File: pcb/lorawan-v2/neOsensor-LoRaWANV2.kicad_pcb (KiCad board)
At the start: 2 copper layers, 49.5 x 49.5 mm, 35 parts, among them J1 Conn_01x05, J2 Conn_01x02, J3 Conn_01x05, J4 Conn_01x04, J5 Conn_01x05, J6 Conn_01x05, J7 Conn_01x05, SW1 G71Y, U1 OLED1.3_I2C, U2 ATECC508A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

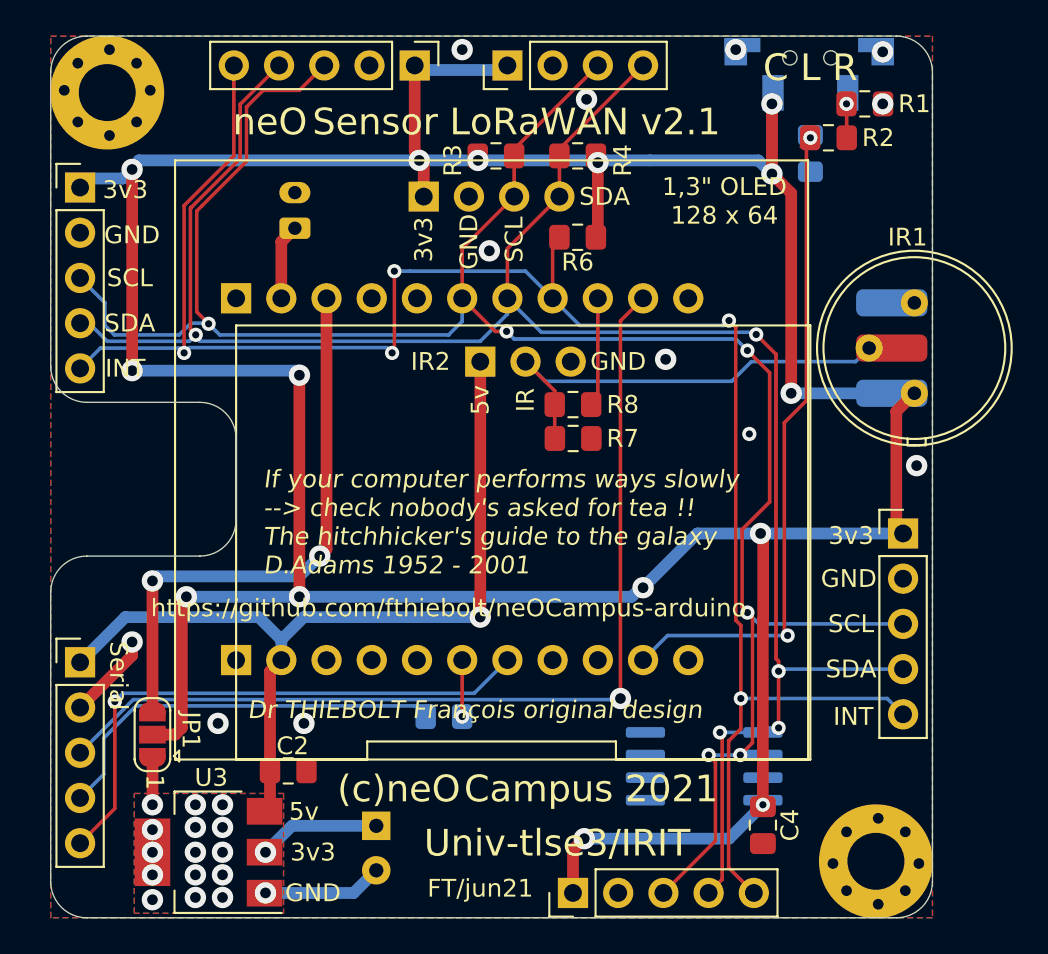
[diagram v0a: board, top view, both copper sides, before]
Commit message: new LoRaWAN V2.1 sent to manufacturing
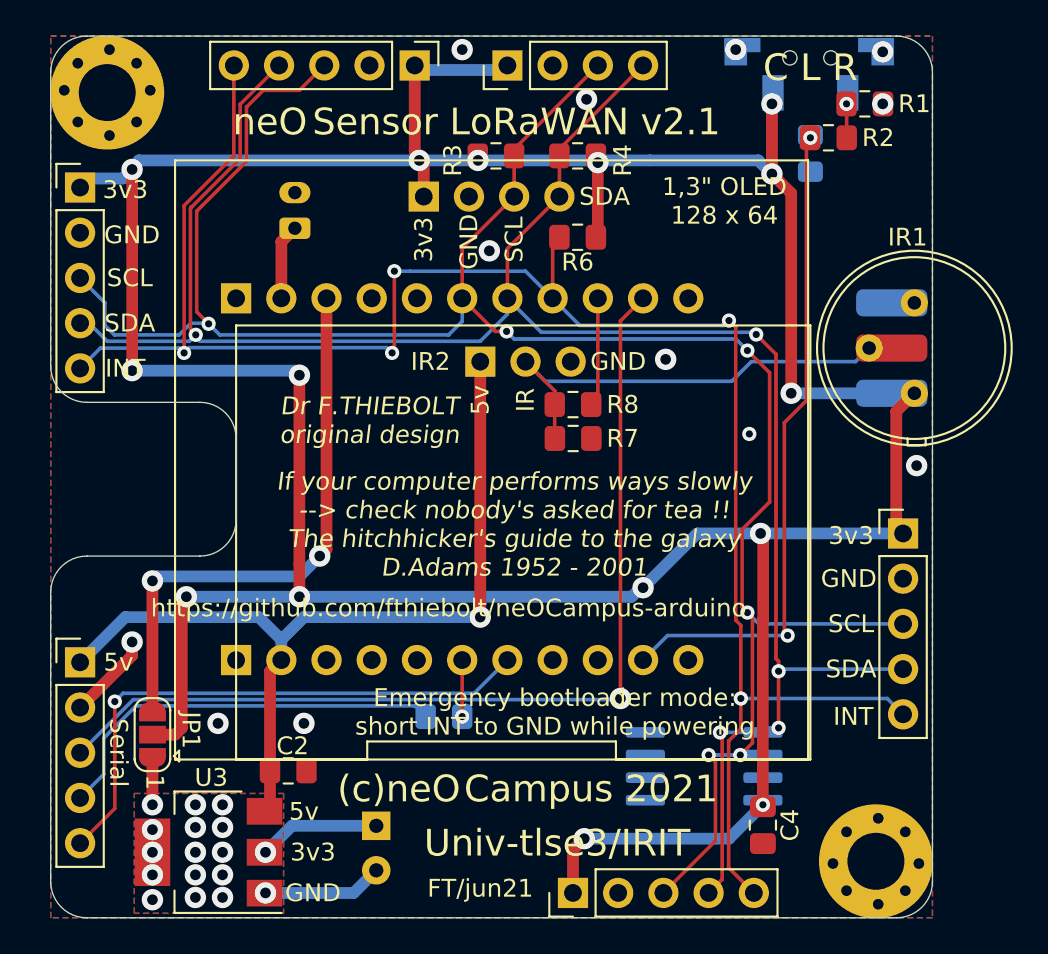
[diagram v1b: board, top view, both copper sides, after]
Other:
- board text added: "Dr F.THIEBOLT original design"
- board text added: "Emergency bootloader mode: short INT to GND while powering"
- board text removed: "Dr THIEBOLT François original design"
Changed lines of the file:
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@@
-(kicad_pcb (version 20171130) (host pcbnew 5.1.10-1.fc34)
+(kicad_pcb (version 20171130) (host pcbnew 5.1.8-1.fc31)
   (general
     (thickness 1.6)
-    (drawings 91)
+    (drawings 93)
     (tracks 312)
     (zones 0)
@@
     )
   )
+  (gr_text "Emergency bootloader mode:\nshort INT to GND while powering" (at 58.547 64.643) (layer F.SilkS)
+    (effects (font (size 1 1) (thickness 0.15)))
+  )
+  (gr_text 5v (at 34.036 61.849) (layer F.SilkS)
+    (effects (font (size 1 1) (thickness 0.15)))
+  )
   (gr_text SDA (at 61.341 35.687) (layer F.SilkS)
     (effects (font (size 1 1) (thickness 0.15)))
@@
     (effects (font (size 1 1) (thickness 0.15)))
   )
-  (gr_text "Dr THIEBOLT François original design" (at 41.275 64.516) (layer F.SilkS)
-    (effects (font (size 1 1) (thickness 0.15) italic) (justify left))
+  (gr_text "Dr F.THIEBOLT\noriginal design" (at 48.133 48.26) (layer F.SilkS)
+    (effects (font (size 1 1) (thickness 0.15) italic))
   )
   (gr_text GND (at 44.958 74.803) (layer F.SilkS)
@@
     (effects (font (size 1 1) (thickness 0.15)))
   )
-  (gr_text "If your computer performs ways slowly\n--> check nobody's asked for tea !!\nThe hitchhicker's guide to the galaxy\nD.Adams 1952 - 2001" (at 42.164 53.975) (layer F.SilkS)
-    (effects (font (size 1 1) (thickness 0.15) italic) (justify left))
+  (gr_text "If your computer performs ways slowly\n--> check nobody's asked for tea !!\nThe hitchhicker's guide to the galaxy\nD.Adams 1952 - 2001" (at 56.261 54.102) (layer F.SilkS)
+    (effects (font (size 1 1) (thickness 0.15) italic))
   )
   (gr_line (start 38.354 63.754) (end 38.481 63.754) (layer B.SilkS) (width 0.12))
@@
   (gr_line (start 49.657 63.754) (end 49.657 68.072) (layer B.SilkS) (width 0.12))
   (gr_line (start 38.481 63.754) (end 49.657 63.754) (layer B.SilkS) (width 0.12))
-  (gr_text "Universities\nare GREAT !" (at 49.403 66.04) (layer B.SilkS)
-    (effects (font (size 1.2 1.2) (thickness 0.2)) (justify left mirror))
+  (gr_text "Universities\nare GREAT !" (at 43.942 65.913) (layer B.SilkS)
+    (effects (font (size 1.2 1.2) (thickness 0.2)) (justify mirror))
   )
   (gr_text GND (at 62.103 44.958) (layer F.SilkS)
@@
     (effects (font (size 1 1) (thickness 0.15)) (justify mirror))
   )
-  (gr_text Serial (at 34.036 62.611 270) (layer F.SilkS)
+  (gr_text Serial (at 34.036 66.929 270) (layer F.SilkS)
     (effects (font (size 1 1) (thickness 0.15)))
   )
@@
     (effects (font (size 1.5 1.5) (thickness 0.3)))
   )
-  (gr_text "CubeCell\nHTCC-AB01" (at 58.547 50.8) (layer B.SilkS)
-    (effects (font (size 2 2) (thickness 0.3)) (justify left mirror))
+  (gr_text "CubeCell\nHTCC-AB01" (at 50.038 51.054) (layer B.SilkS)
+    (effects (font (size 2 2) (thickness 0.3)) (justify mirror))
   )
   (gr_text FT/jun21 (at 54.356 74.549) (layer F.SilkS)
